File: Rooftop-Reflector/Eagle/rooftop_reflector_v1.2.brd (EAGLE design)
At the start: 172.7 x 106.4 mm, 12 parts, among them Q4 MOSFET-NCH, U1 ADAFRUIT_LEONARDO, X1 MSTBA4, X2 MSTBA5, X3 MSTBA3

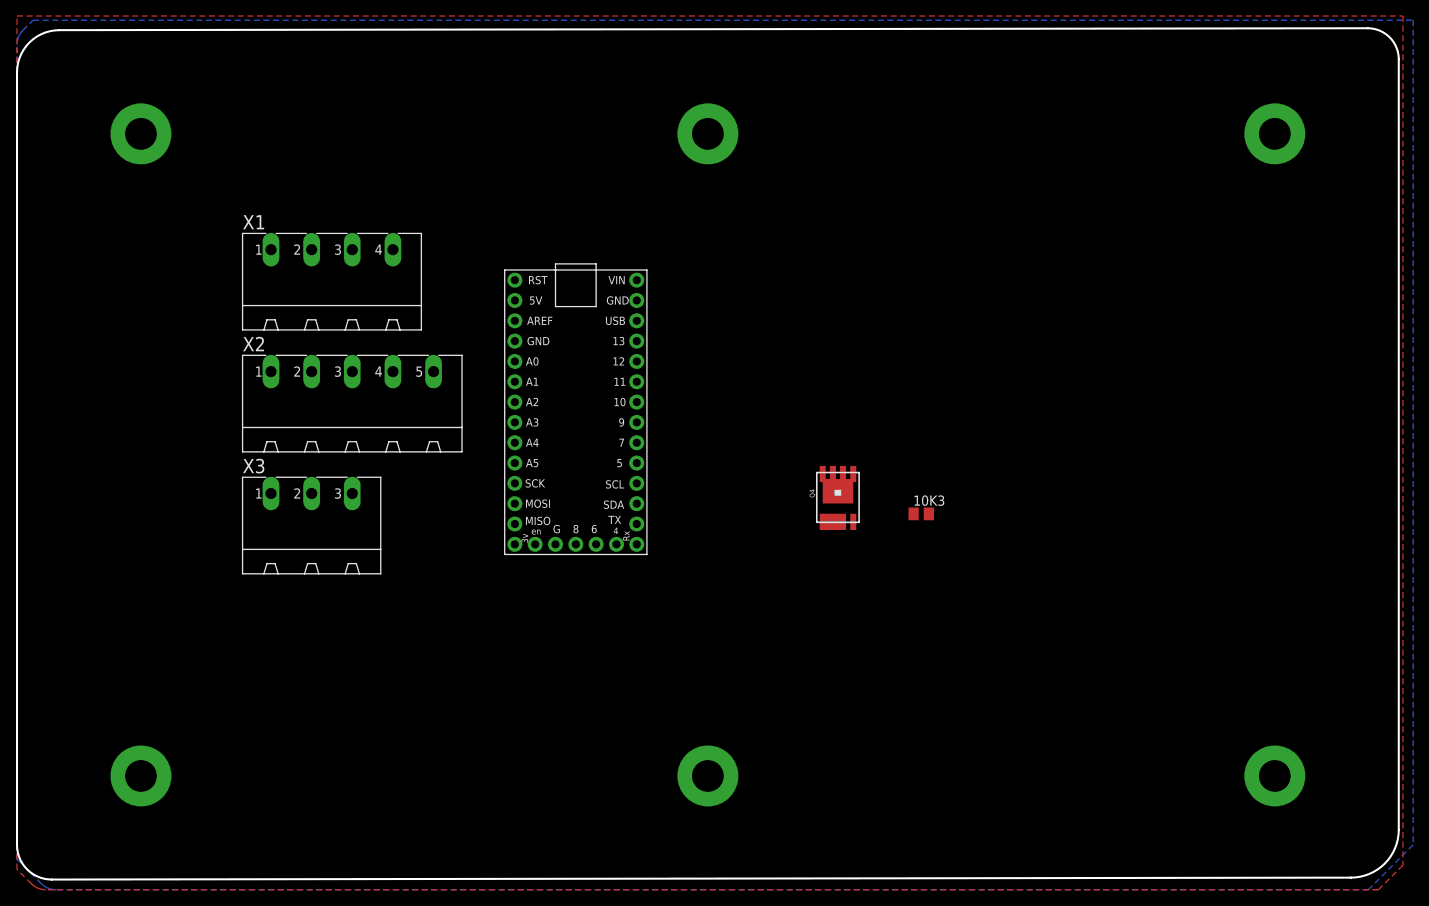
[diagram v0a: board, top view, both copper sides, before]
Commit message: Updated Btn calls and added Pulse function
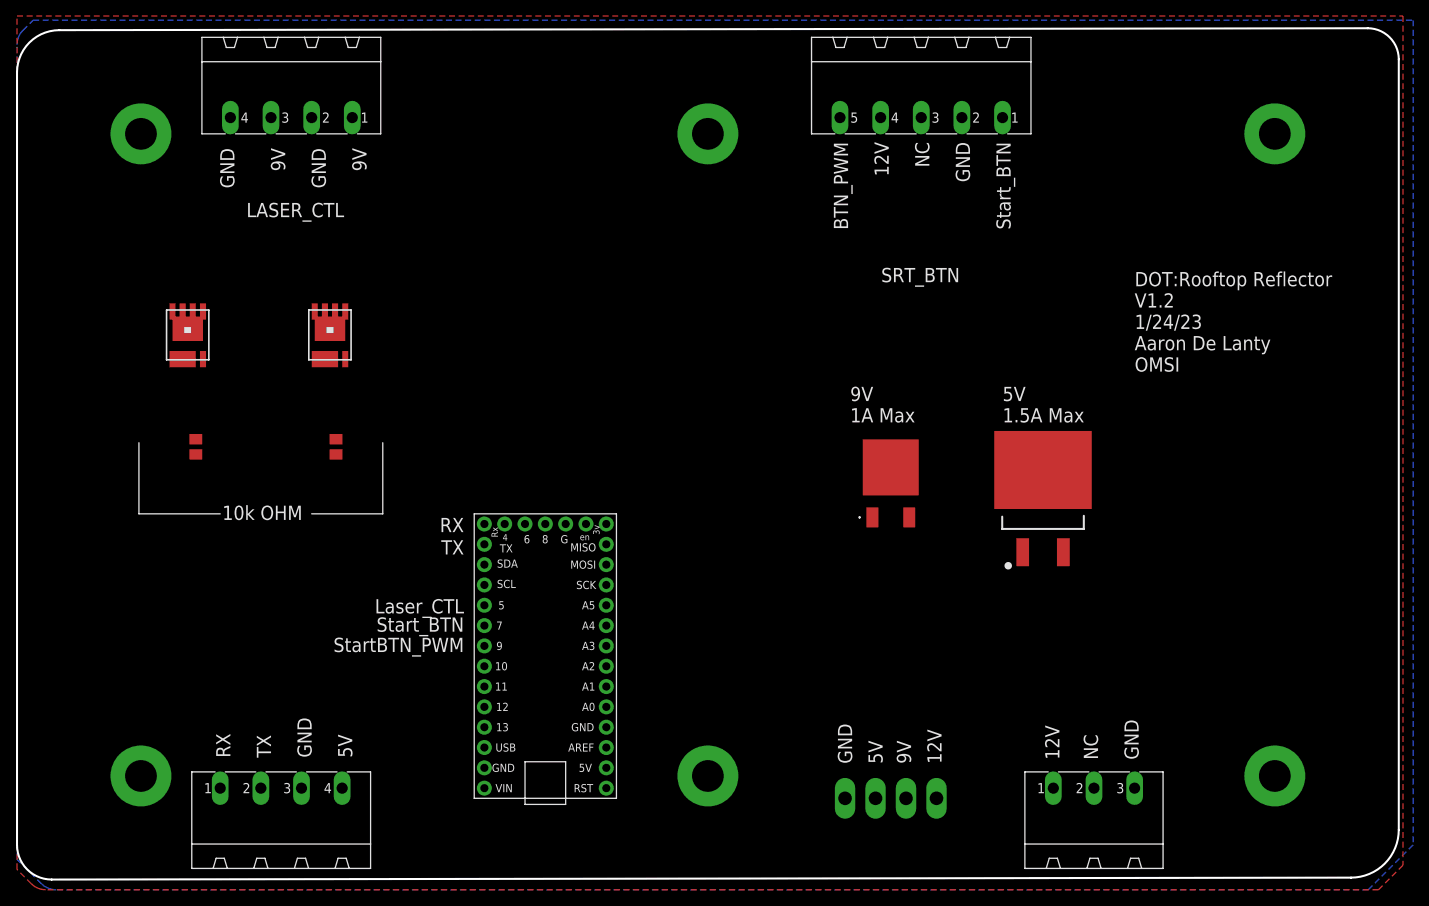
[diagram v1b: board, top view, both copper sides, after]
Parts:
- removed X2: MSTBA5, con-phoenix-508:MSTBA5
- removed X3: MSTBA3, con-phoenix-508:MSTBA3
- added 10K1: (no value), adafruit:M0805
- added 12VIN: MSTBA3, con-phoenix-508:MSTBA3
- added 5V: L7805ABD2T-TR, SamacSys_Parts:D2PAK-STB35NF10T4
- added 9V: BA17809FP-E2, SamacSys_Parts:BA17809FPE2
- added LASER_CTL: MSTBA4, con-phoenix-508:MSTBA4
- added Q1: MOSFET-NCH, th_ds_libraries:SO-8_POWER_PAK
- added SRT_BTN: MSTBA5, con-phoenix-508:MSTBA5
- added TP1, TP2: PTR2, testpad:P2-38-17
- moved 10K3 73.6 mm to (28.4, 55.4), turned to 270 degrees
- moved X1 67.6 mm to (21.6, 7.62)
- moved Q4 66.7 mm to (29.2, 69.8)
- moved U1 41.6 mm to (52.1, 24.1), turned to 180 degrees
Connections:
- removed net N$1: 10K3.2
- removed net N$10: Q4.D1
- new net 12V: 12VIN.1, 5V.1, 9V.1, SRT_BTN.4, TP2.TP-1
- new net 5V: 5V.3, TP1.TP-2, U1.VIN, X1.4
- new net 9V: 9V.3, LASER_CTL.1, LASER_CTL.3, TP2.TP-2
- new net D5: 10K1.2, U1.D5
- new net D7: SRT_BTN.1, U1.D7
- new net D9: 10K3.2, U1.D9
- new net LZR_CTL: LASER_CTL.2, LASER_CTL.4, Q1.D1
- new net N$4: 10K1.1, Q1.G
- new net N$7: U1.TX, X1.2
- new net N$8: U1.RX, X1.1
- new net SRT_PWM: Q4.D1, SRT_BTN.5
- net GND: now also 12VIN.3, 5V.4, 9V.2, Q1.S, SRT_BTN.2, TP1.TP-1, U1.GND@0, U1.GND@2, X1.3
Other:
- board text added: "10k OHM"
- board text added: "12V"
- board text added: "5V"
- board text added: "5V 1.5A Max"
- board text added: "9V"
- board text added: "9V 1A Max"
- board text added: "BTN_PWM"
- board text added: "DOT:Rooftop Reflector V1.2 1/24/23 Aaron De Lanty OMSI"
- board text added: "GND"
- board text added: "Laser_CTL"
- board text added: "NC"
- board text added: "RX"
- board text added: "StartBTN_PWM"
- board text added: "Start_BTN"
- board text added: "TX"
